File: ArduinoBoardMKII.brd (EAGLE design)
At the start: 95.2 x 82.5 mm, 29 parts

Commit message: Update
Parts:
- added JP1, JP2: (no value), jumper:JP2
- turned R10 to 0 degrees
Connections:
- new net 5V: JP1.1, JP2.1
- new net N$12: JP2.2, R9.2
- new net N$13: JP1.3
- new net N$21: JP2.3
- new net N$4: JP1.2, R10.2
- net +5V: no longer R9.2
- net GND: no longer R10.1
- net MOTOR-IN2: now also R10.1; no longer R10.2
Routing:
- net +5V: track 111.4 -> 87.7 mm
- net MOTOR-IN2: track 26.3 -> 3.30 mm
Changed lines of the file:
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@@
 <attribute name="VALUE" x="50.419" y="42.4942" size="1.27" layer="27" ratio="10"/>
 </element>
-<element name="R10" library="resistor" library_urn="urn:adsk.eagle:library:348" package="0207/12" package3d_urn="urn:adsk.eagle:package:25938/1" value="47k" x="52.705" y="55.88" rot="R180">
-<attribute name="NAME" x="55.88" y="54.483" size="1.27" layer="25" ratio="10" rot="R180"/>
-<attribute name="VALUE" x="54.991" y="56.5658" size="1.27" layer="27" ratio="10" rot="R180"/>
+<element name="R10" library="resistor" library_urn="urn:adsk.eagle:library:348" package="0207/12" package3d_urn="urn:adsk.eagle:package:25938/1" value="47k" x="52.705" y="55.88">
+<attribute name="NAME" x="49.53" y="57.277" size="1.27" layer="25" ratio="10"/>
+<attribute name="VALUE" x="50.419" y="55.1942" size="1.27" layer="27" ratio="10"/>
 </element>
 <element name="12V" library="con-phoenix-smkdsp" library_urn="urn:adsk.eagle:library:180" package="SMKDSP_1,5/2" package3d_urn="urn:adsk.eagle:package:9814/1" value="SMKDSP_1,5/2" x="87.63" y="26.67" rot="R90">
@@
 <element name="R4" library="adafruit" package="0207/10" value="220" x="32.385" y="76.835"/>
 <element name="R5" library="adafruit" package="0207/10" value="100" x="66.675" y="73.025" rot="R180"/>
+<element name="JP1" library="jumper" library_urn="urn:adsk.eagle:library:252" package="JP2" package3d_urn="urn:adsk.eagle:package:15452/1" value="" x="-6.35" y="3.81"/>
+<element name="JP2" library="jumper" library_urn="urn:adsk.eagle:library:252" package="JP2" package3d_urn="urn:adsk.eagle:package:15452/1" value="" x="-14.605" y="3.81"/>
 </elements>
 <signals>
@@
 <contactref element="VNH5019" pad="GND2"/>
 <contactref element="VNH5019" pad="GND1"/>
-<contactref element="R10" pad="1"/>
 <contactref element="VIN" pad="2"/>
 <contactref element="VNH5019" pad="GND4"/>
@@
 <contactref element="LED1" pad="COMMON_CATHODE"/>
 <contactref element="R5" pad="1"/>
-<wire x1="71.755" y1="71.12" x2="71.755" y2="74.93" width="0" layer="19" extent="1-1"/>
+<wire x1="71.755" y1="73.025" x2="71.755" y2="74.93" width="0" layer="19" extent="1-1"/>
+<wire x1="71.755" y1="71.12" x2="71.755" y2="73.025" width="0" layer="19" extent="1-1"/>
 <wire x1="65.405" y1="67.31" x2="71.755" y2="71.12" width="0" layer="19" extent="1-1"/>
 <wire x1="65.405" y1="62.865" x2="65.405" y2="67.31" width="0" layer="19" extent="1-1"/>
-<wire x1="59.055" y1="55.88" x2="65.405" y2="62.865" width="0" layer="19" extent="1-1"/>
-<wire x1="65.405" y1="53.34" x2="59.055" y2="55.88" width="0" layer="19" extent="1-1"/>
+<wire x1="65.405" y1="53.34" x2="65.405" y2="62.865" width="0" layer="19" extent="1-1"/>
 <wire x1="66.04" y1="49.53" x2="65.405" y2="53.34" width="0" layer="19" extent="1-1"/>
 <wire x1="65.405" y1="45.72" x2="66.04" y2="49.53" width="0" layer="19" extent="1-1"/>
@@
 <wire x1="88.265" y1="53.34" x2="87.63" y2="46.99" width="0" layer="19" extent="1-1"/>
 <wire x1="84.455" y1="56.515" x2="88.265" y2="53.34" width="0" layer="19" extent="1-1"/>
-<wire x1="48.26" y1="62.865" x2="59.055" y2="55.88" width="0" layer="19" extent="1-1"/>
+<wire x1="66.04" y1="8.255" x2="78.74" y2="11.43" width="0" layer="19" extent="1-1"/>
+<wire x1="48.26" y1="62.865" x2="65.405" y2="62.865" width="0" layer="19" extent="1-1"/>
 <wire x1="45.72" y1="60.325" x2="48.26" y2="62.865" width="0" layer="19" extent="1-1"/>
 <wire x1="42.545" y1="61.595" x2="45.72" y2="60.325" width="0" layer="19" extent="1-1"/>
@@
 <wire x1="38.735" y1="57.785" x2="40.64" y2="59.69" width="0" layer="19" extent="1-1"/>
 <wire x1="36.195" y1="55.245" x2="38.735" y2="57.785" width="0" layer="19" extent="1-1"/>
-<wire x1="43.860125" y1="54.655125" x2="40.64" y2="59.69" width="0" layer="19" extent="1-1"/>
+<wire x1="43.860125" y1="54.655125" x2="45.72" y2="60.325" width="0" layer="19" extent="1-1"/>
 <wire x1="44.495125" y1="47.670125" x2="43.860125" y2="54.655125" width="0" layer="19" extent="1-1"/>
 <wire x1="38.1" y1="40.64" x2="44.495125" y2="47.670125" width="0" layer="19" extent="1-1"/>
@@
 <wire x1="26.67" y1="10.795" x2="30.48" y2="10.795" width="0" layer="19" extent="1-1"/>
 <wire x1="26.67" y1="7.62" x2="26.67" y2="10.795" width="0" layer="19" extent="1-1"/>
-<wire x1="46.0600625" y1="74.852959375" x2="48.26" y2="62.865" width="0" layer="19" extent="1-1"/>
 <wire x1="24.765" y1="30.48" x2="36.83" y2="29.845" width="0" layer="19" extent="1-1"/>
 <wire x1="24.765" y1="29.21" x2="24.765" y2="30.48" width="0" layer="19" extent="1-1"/>
@@
 <wire x1="3.175" y1="49.53" x2="3.175" y2="46.99" width="0" layer="19" extent="1-1"/>
 <wire x1="3.175" y1="57.15" x2="3.175" y2="49.53" width="0" layer="19" extent="1-1"/>
+<wire x1="4.445" y1="59.055" x2="3.175" y2="57.15" width="0" layer="19" extent="1-1"/>
 <wire x1="1.905" y1="59.055" x2="3.175" y2="57.15" width="0" layer="19" extent="1-1"/>
-<wire x1="4.445" y1="59.055" x2="3.175" y2="57.15" width="0" layer="19" extent="1-1"/>
-<wire x1="66.04" y1="8.255" x2="78.74" y2="11.43" width="0" layer="19" extent="1-1"/>
+<wire x1="46.0600625" y1="74.852959375" x2="48.26" y2="62.865" width="0" layer="19" extent="1-1"/>
 <wire x1="5.08" y1="16.51" x2="13.335" y2="26.67" width="0" layer="19" extent="1-1"/>
 <wire x1="7.62" y1="14.605" x2="5.08" y2="16.51" width="0" layer="19" extent="1-1"/>
-<wire x1="71.755" y1="73.025" x2="7.62" y2="14.605" width="0" layer="19" extent="1-1"/>
 </signal>
 <signal name="+12V">
@@
 <signal name="MOTOR-IN2">
 <contactref element="R8" pad="1"/>
-<contactref element="R10" pad="2"/>
 <contactref element="MICRO" pad="D11"/>
-<wire x1="46.355" y1="55.88" x2="46.355" y2="52.07" width="0.635" layer="1"/>
-<wire x1="46.355" y1="55.88" x2="40.005" y2="62.23" width="0.635" layer="1"/>
-<wire x1="40.005" y1="62.23" x2="29.845" y2="62.23" width="0.635" layer="1"/>
 <contactref element="J2" pad="6"/>
 <wire x1="26.67" y1="62.23" x2="29.972" y2="62.23" width="0.8128" layer="1"/>
-<wire x1="29.972" y1="62.23" x2="29.845" y2="62.23" width="0" layer="19" extent="1-1"/>
+<contactref element="R10" pad="1"/>
+<wire x1="46.355" y1="52.07" x2="46.355" y2="55.88" width="0" layer="19" extent="1-1"/>
+<wire x1="29.972" y1="62.23" x2="46.355" y2="52.07" width="0" layer="19" extent="1-1"/>
 </signal>
 <signal name="MOTOR-IN1">
@@
 <signal name="+5V">
 <contactref element="VNH5019" pad="VDD"/>
-<contactref element="R9" pad="2"/>
 <contactref element="SWITCH" pad="2"/>
 <wire x1="15.24" y1="36.83" x2="15.24" y2="7.62" width="1.27" layer="1"/>
@@
 <wire x1="35.191875" y1="3.048" x2="38.4302" y2="6.286325" width="1.016" layer="1"/>
 <wire x1="45.085" y1="24.13" x2="42.545" y2="24.13" width="1.27" layer="1"/>
-<wire x1="59.055" y1="43.18" x2="45.085" y2="24.13" width="1.27" layer="1"/>
 <wire x1="15.24" y1="7.62" x2="15.24" y2="6.35" width="1.27" layer="1"/>
 <wire x1="15.24" y1="6.35" x2="18.542" y2="3.048" width="1.016" layer="1"/>
 <wire x1="18.542" y1="3.048" x2="35.191875" y2="3.048" width="1.016" layer="1"/>
-<wire x1="6.35" y1="51.435" x2="6.35" y2="43.18" width="0" layer="19" extent="1-16"/>
-<wire x1="6.35" y1="51.435" x2="5.715" y2="52.07" width="0" layer="19" extent="1-16"/>
-<wire x1="6.35" y1="43.18" x2="5.08" y2="41.91" width="0" layer="19" extent="1-16"/>
-<wire x1="5.715" y1="36.83" x2="5.715" y2="41.275" width="0" layer="19" extent="1-16"/>
-<wire x1="5.715" y1="41.275" x2="5.08" y2="41.91" width="0" layer="19" extent="1-16"/>
 <wire x1="42.545" y1="24.13" x2="38.4302" y2="24.13" width="1.016" layer="1"/>
 <contactref element="MICRO" pad="5V"/>
@@
 <wire x1="11.43" y1="36.83" x2="8.382" y2="36.83" width="1.27" layer="1"/>
 <wire x1="11.43" y1="36.83" x2="15.24" y2="36.83" width="1.27" layer="1"/>
-<wire x1="8.382" y1="36.83" x2="5.715" y2="36.83" width="0" layer="19" extent="1-16"/>
 </signal>
 <signal name="SCL">
@@
 <wire x1="5.969" y1="51.181" x2="5.969" y2="52.959" width="0.8128" layer="1"/>
 </signal>
+<signal name="N$4">
+<contactref element="R10" pad="2"/>
+<contactref element="JP1" pad="2"/>
+<wire x1="-6.35" y1="3.81" x2="59.055" y2="55.88" width="0" layer="19" extent="1-1"/>
+</signal>
+<signal name="N$12">
+<contactref element="R9" pad="2"/>
+<contactref element="JP2" pad="2"/>
+<wire x1="-14.605" y1="3.81" x2="59.055" y2="43.18" width="0" layer="19" extent="1-1"/>
+</signal>
+<signal name="N$13">
+<contactref element="JP1" pad="3"/>
+</signal>
+<signal name="N$21">
+<contactref element="JP2" pad="3"/>
+</signal>
+<signal name="5V">
+<contactref element="JP2" pad="1"/>
+<contactref element="JP1" pad="1"/>
+<wire x1="-8.89" y1="3.81" x2="-17.145" y2="3.81" width="0" layer="19" extent="1-1"/>
+</signal>
 </signals>

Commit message: Buzzer Progress
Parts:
- added J5: (no value), SparkFun-Connectors:1X02
- added SG1: F/QMB, buzzer:F/QMB
- moved JP1 86.7 mm to (54.6, 65.4)
- moved JP2 79.9 mm to (54.6, 43.8)
- moved GND 14.0 mm to (80.0, 8.26)
- moved R3 11.7 mm to (24.1, 17.1), turned to 0 degrees
- moved SWITCH 10.8 mm to (28.6, 6.99)
- moved CPC1718 6.35 mm to (65.4, 71.8)
- moved R5 5.08 mm to (66.7, 78.1)
- moved R7 5.08 mm to (52.7, 52.1)
- moved R9 5.08 mm to (52.7, 48.3)
- moved R8 3.81 mm to (52.7, 55.9)
- moved R10 3.81 mm to (52.7, 59.7)
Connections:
- net N$17 renamed BUZZER
- removed net 5V: JP1.1, JP2.1
- removed net N$13: JP1.3
- removed net N$21: JP2.3
- net +5V: now also JP1.1, JP2.1
- net GND: now also JP1.3, JP2.3
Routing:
- net +5V: track 87.7 -> 126.9 mm
- net MOTOR-IN2: track 3.30 -> 24.6 mm
- net SDA: track 37.4 -> 49.4 mm
- net N$4: track 0.00 -> 7.56 mm
- net N$12: track 0.00 -> 6.48 mm
- net POST-OPTO-DIODE: track 0.00 -> 6.35 mm
- net DOORSWITCH: track 51.9 -> 56.4 mm
- net RELAY-TO-MOTORCONTROLLER: track 15.8 -> 20.2 mm
- net MOTOR-IN1: track 31.2 -> 28.6 mm
- net +12V: track 85.9 -> 88.6 mm
- net IN1: track 10.4 -> 11.9 mm
- net IN2: track 10.00 -> 11.6 mm
- net MOTOR-ENABLE: track 51.6 -> 50.1 mm
- net MOTOR-ERRORFLAG: track 56.0 -> 56.7 mm
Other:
- board text added: "5V IN1 GND"
- board text added: "5V IN2 GND"

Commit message: Update
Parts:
- added R1: 1k, rcl:0207/7
- added T1: 2N2222, transistor:TO18
- R11, R6: value 38k -> 47k
- R5: value 100 -> 330
- moved R3 1.42 mm to (23.5, 18.4)
- moved SWITCH 1.27 mm to (29.8, 6.99)
- moved SDA__SCL2 1.27 mm to (34.3, 6.99)
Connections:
- new net N$13: SG1.-, T1.3
- new net N$17: R1.2, T1.2
- net +5V: now also SG1.+
- net BUZZER: now also R1.1
- net GND: now also T1.1
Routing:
- net BUZZER: track 3.30 -> 54.0 mm, vias 0 -> 2
- net N$13: track 0.00 -> 10.5 mm
- net +5V: track 126.9 -> 132.7 mm
- net N$17: track 0.00 -> 3.17 mm
- net RGBD-GREEN: track 36.1 -> 38.7 mm
- net RGBD-BLUE: track 27.9 -> 28.8 mm
- net DOORSWITCH: track 56.4 -> 57.2 mm
- net SCL: track 53.2 -> 52.4 mm
- net MOTOR-ENABLE: track 50.1 -> 50.6 mm

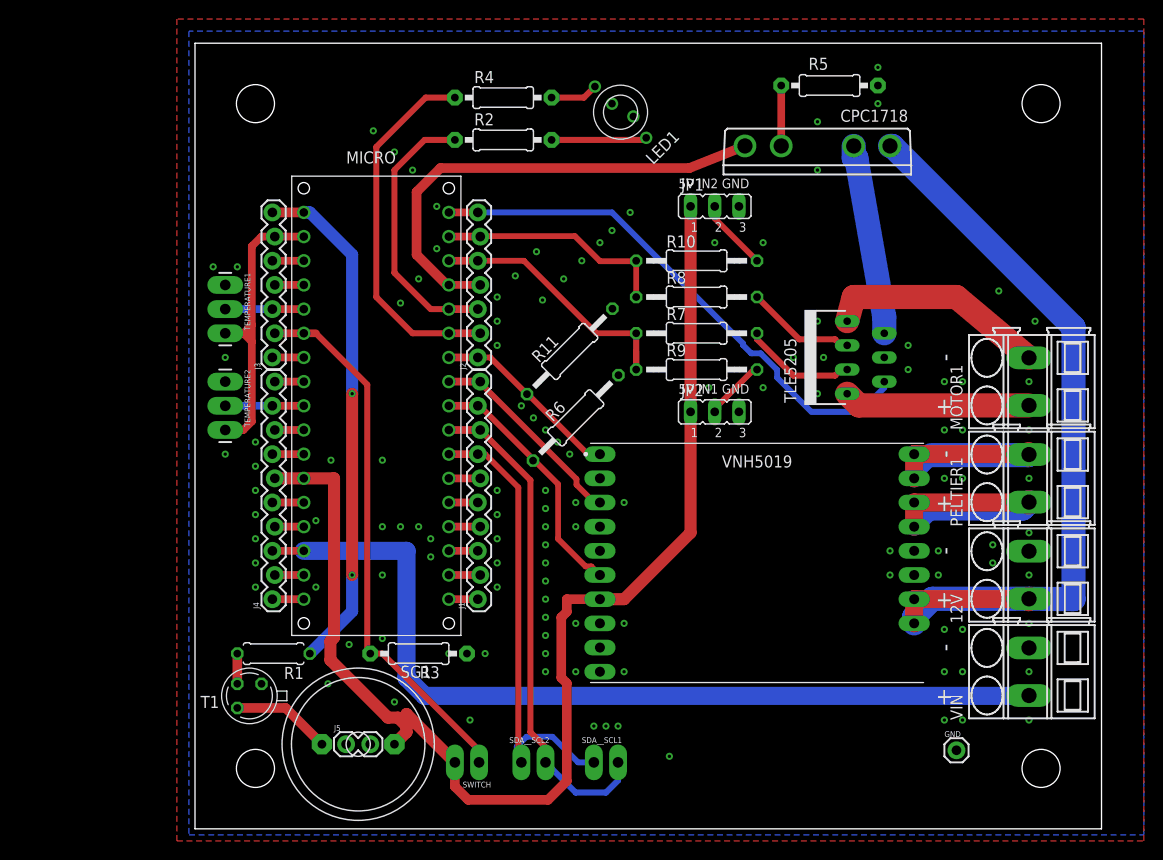
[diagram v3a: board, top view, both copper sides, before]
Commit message: Updated Arduino wih correct grounding and board size.
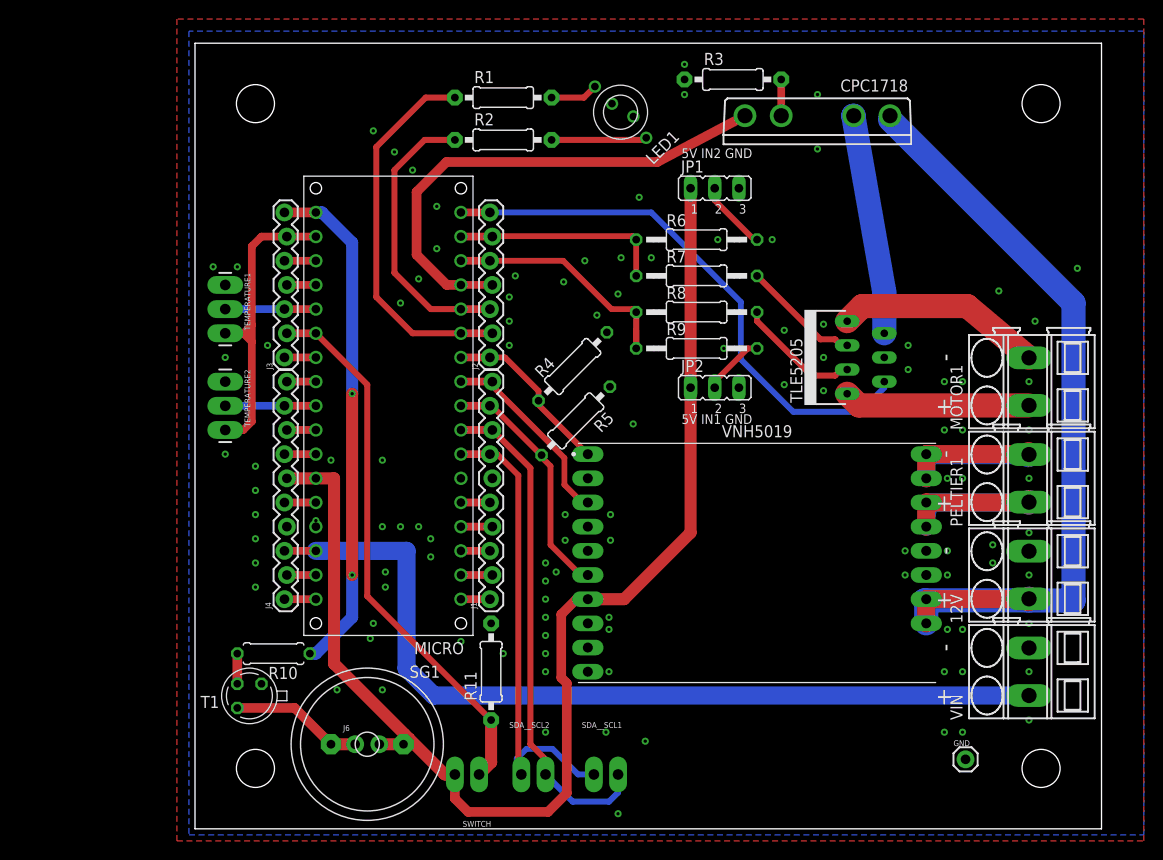
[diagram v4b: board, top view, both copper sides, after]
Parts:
- removed J5: (no value), SparkFun-Connectors:1X02
- added J6: (no value), SparkFun-Connectors:1X02_NO_SILK
- R1: value 1k -> 220; device rcl:0207/7 -> adafruit:0207/10
- R10: value 47k -> 1k; device resistor:0207/12 -> rcl:0207/7
- R11: value 47k -> 4.7k; device resistor:0207/12 -> adafruit:0207/10
- R3: value 4.7k -> 330
- R4: value 220 -> 47k; device adafruit:0207/10 -> resistor:0207/10
- R5: value 330 -> 47k; device adafruit:0207/10 -> resistor:0207/10
- moved R3 68.8 mm to (56.5, 78.7)
- moved R1 63.2 mm to (32.4, 76.8), turned to 0 degrees
- moved R10 60.7 mm to (8.26, 18.4), turned to 180 degrees
- moved R5 44.2 mm to (40.0, 42.9), turned to 225 degrees
- moved R11 34.7 mm to (31.1, 16.5), turned to 90 degrees
- moved R4 29.2 mm to (39.7, 48.6), turned to 45 degrees
- moved R6 22.6 mm to (52.7, 61.9), turned to 0 degrees
- moved R7 6.03 mm to (52.7, 58.1)
- moved CPC1718 3.18 mm to (65.4, 74.9)
- moved JP2 2.54 mm to (54.6, 46.4)
- moved R9 2.22 mm to (52.7, 50.5)
- moved JP1 1.91 mm to (54.6, 67.3)
- moved R8 1.59 mm to (52.7, 54.3)
- moved GND 1.35 mm to (81.0, 7.30)
- moved SDA__SCL1 1.27 mm to (41.9, 5.71)
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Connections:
- removed net N$1: J4.4, MICRO.GND1
- removed net N$5: J1.6, MICRO.GND
- net +5V: now also J6.2
- net BUZZER: now also R10.1; no longer R1.1
- net DOORSWITCH: now also R11.1; no longer R3.1
- net GND: now also J1.6, J4.4, MICRO.GND, MICRO.GND1, R3.1, R4.2; no longer R3.2, R6.1
- net IN1: now also R8.2; no longer R7.2
- net IN2: now also R7.2; no longer R8.2
- net MOTOR-IN1: now also R8.1; no longer R7.1
- net MOTOR-IN2: now also R6.1, R7.1; no longer R10.1, R8.1
- net N$13: now also J6.1
- net N$17: now also R10.2; no longer R1.2
- net N$3: now also R1.2; no longer R4.2
- net N$4: now also R6.2; no longer R10.2
- net PELTIER-INA: now also R4.1; no longer R11.1
- net PELTIER-INB: now also R5.2; no longer R6.2
- net POST-OPTO-DIODE: now also R3.2; no longer R5.2
- net RGBD-GREEN: now also R1.1; no longer R4.1
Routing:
- net N$13: track 10.5 -> 14.0 mm
- net N$5: track 3.30 -> 0.00 mm
- net N$1: track 3.05 -> 0.00 mm
- net RELAY-TO-MOTORCONTROLLER: track 20.2 -> 23.2 mm
- net POST-OPTO-DIODE: track 6.35 -> 3.81 mm
- net MOTOR-ENABLE: track 50.6 -> 52.9 mm
- net MOTOR-IN2: track 24.6 -> 22.4 mm
- net MOTOR-IN1: track 28.6 -> 26.4 mm
- net +12V: track 88.6 -> 90.5 mm
- net VIN: track 93.6 -> 91.8 mm
- net MOTOR-ERRORFLAG: track 56.7 -> 58.4 mm
- net MOTOR-OUT2: track 23.4 -> 21.7 mm
- net PELTIER-INA: track 20.1 -> 18.6 mm
- net PELTIER-OUTA: track 28.1 -> 26.6 mm
- net PELTIER-OUTB: track 27.8 -> 26.3 mm
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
